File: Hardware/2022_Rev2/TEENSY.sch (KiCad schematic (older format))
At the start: 1 part

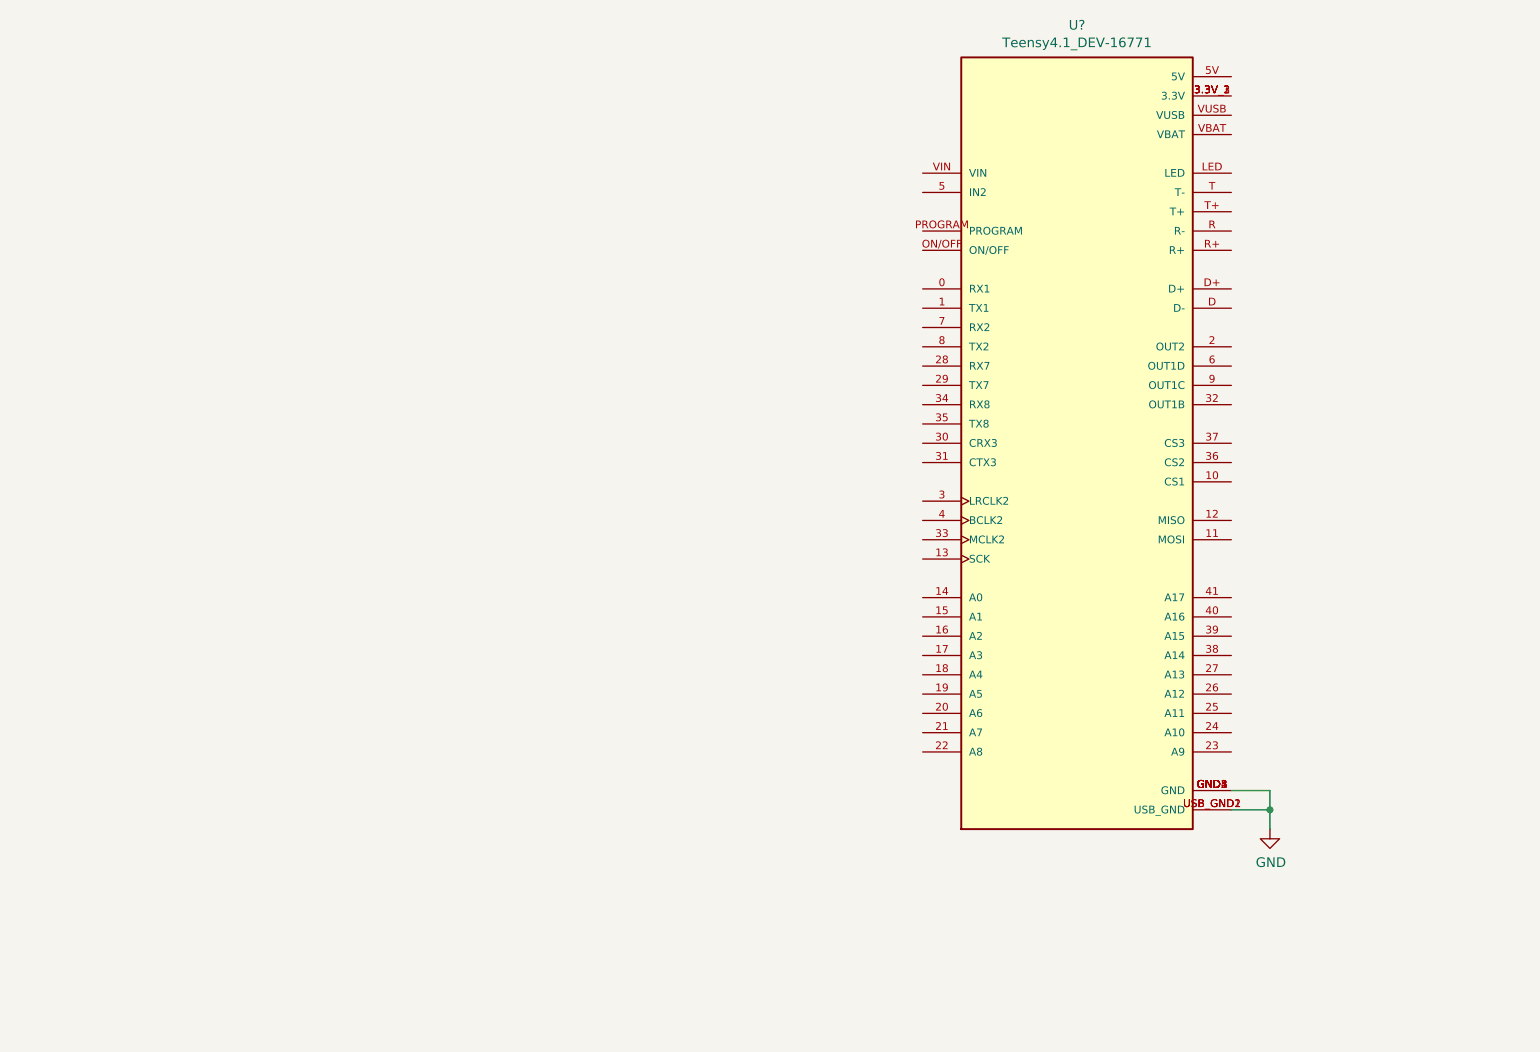
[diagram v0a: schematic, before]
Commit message: Organized some stuff and added Teensy connections
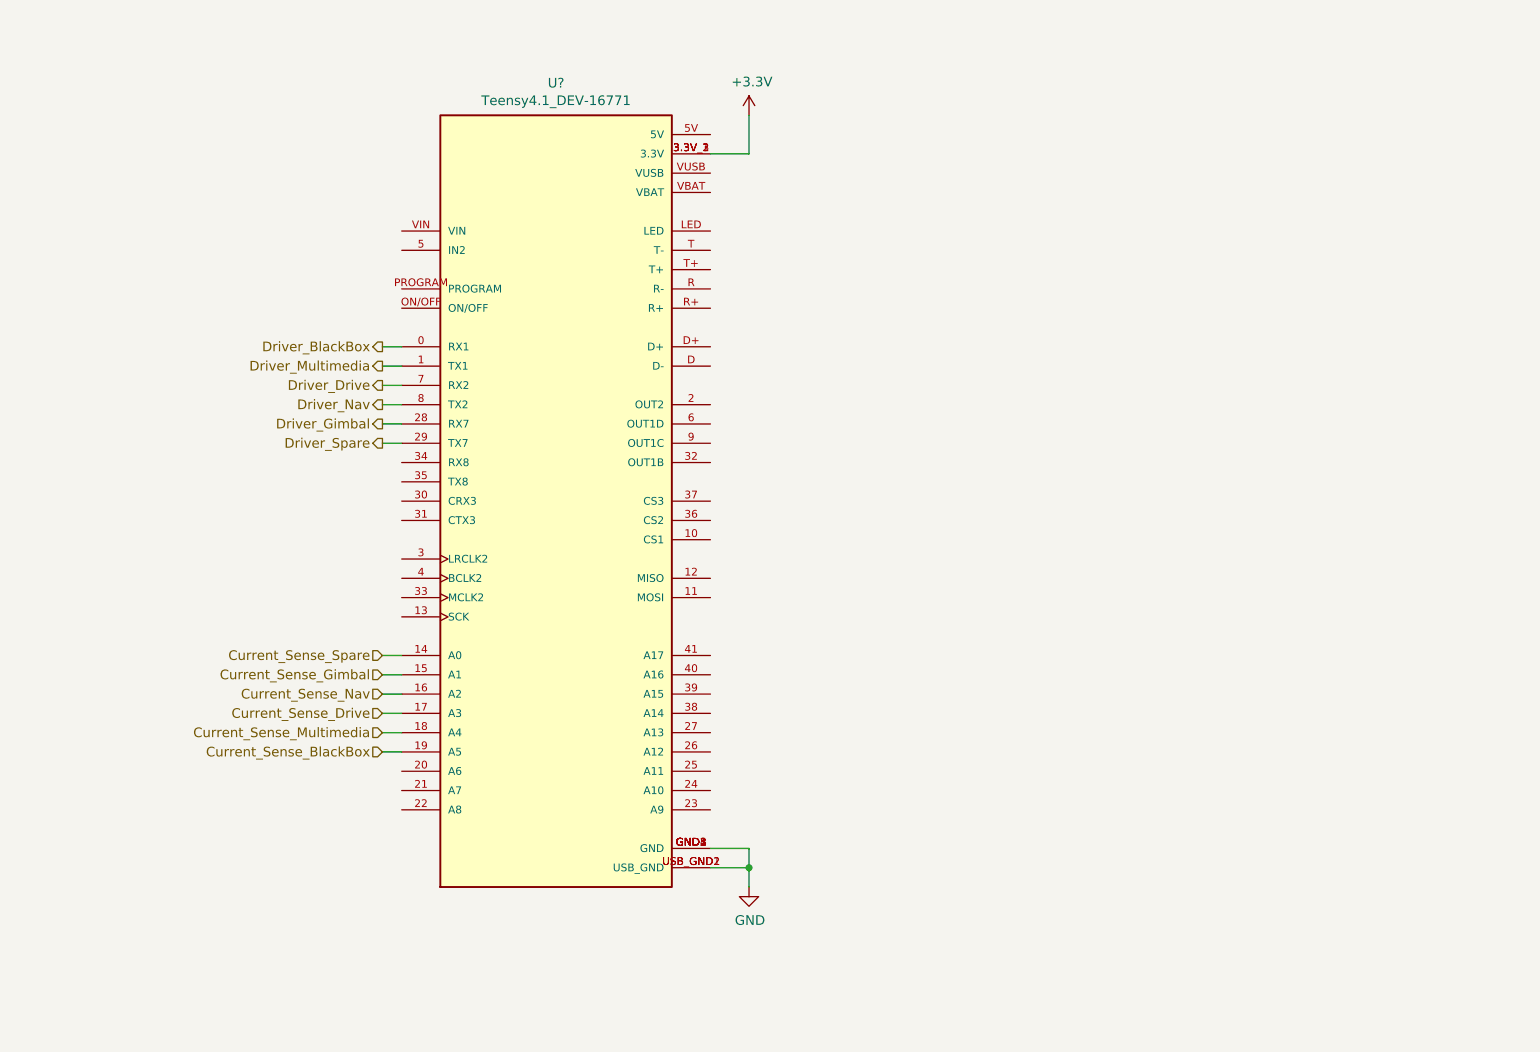
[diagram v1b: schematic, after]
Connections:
- net Driver_BlackBox: now reaches U?.0 (RX1)
- net Driver_Multimedia: now reaches U?.1 (TX1)
- net Current_Sense_Spare: now reaches U?.14 (A0)
- net Current_Sense_Gimbal: now reaches U?.15 (A1)
- net Current_Sense_Nav: now reaches U?.16 (A2)
- net Current_Sense_Drive: now reaches U?.17 (A3)
- net Current_Sense_Multimedia: now reaches U?.18 (A4)
- net Current_Sense_BlackBox: now reaches U?.19 (A5)
- net Driver_Gimbal: now reaches U?.28 (RX7)
- net Driver_Spare: now reaches U?.29 (TX7)
- net +3V3: now reaches U?.3.3V_1 (3.3V), U?.3.3V_2 (3.3V), U?.3.3V_3 (3.3V)
- net Driver_Drive: now reaches U?.7 (RX2)
- net Driver_Nav: now reaches U?.8 (TX2)
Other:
- moved on the sheet: U?
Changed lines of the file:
@@
 EESchema Schematic File Version 4
+LIBS:2022_Rev2-cache
 EELAYER 30 0
 EELAYER END
@@
 L 2022_Rev2-rescue:Teensy4.1_DEV-16771-MRDT_Shields U?
 U 1 1 6211982F
-P 8000 3250
-F 0 "U?" H 8000 5417 50  0000 C CNN
-F 1 "Teensy4.1_DEV-16771" H 8000 5326 50  0000 C CNN
-F 2 "MODULE_DEV-16771" H 10100 2950 50  0001 L BNN
-F 3 "" H 8000 3250 50  0001 L BNN
-F 4 "Manufacturer recommendations" H 10100 2700 50  0001 L BNN "STANDARD"
-F 5 "4.07mm" H 10350 2500 50  0001 L BNN "MAXIMUM_PACKAGE_HEIGHT"
-F 6 "SparkFun Electronics" H 10300 2350 50  0001 L BNN "MANUFACTURER"
-F 7 "4.1" H 7700 1050 50  0001 L BNN "PARTREV"
-	1    8000 3250
+P 5300 3550
+F 0 "U?" H 5300 5717 50  0000 C CNN
+F 1 "Teensy4.1_DEV-16771" H 5300 5626 50  0000 C CNN
+F 2 "MODULE_DEV-16771" H 7400 3250 50  0001 L BNN
+F 3 "" H 5300 3550 50  0001 L BNN
+F 4 "Manufacturer recommendations" H 7400 3000 50  0001 L BNN "STANDARD"
+F 5 "4.07mm" H 7650 2800 50  0001 L BNN "MAXIMUM_PACKAGE_HEIGHT"
+F 6 "SparkFun Electronics" H 7600 2650 50  0001 L BNN "MANUFACTURER"
+F 7 "4.1" H 5000 1350 50  0001 L BNN "PARTREV"
+	1    5300 3550
 	1    0    0    -1
 $EndComp
@@
 L power:GND #PWR?
 U 1 1 62120694
-P 9000 5250
-F 0 "#PWR?" H 9000 5000 50  0001 C CNN
-F 1 "GND" H 9005 5077 50  0000 C CNN
-F 2 "" H 9000 5250 50  0001 C CNN
-F 3 "" H 9000 5250 50  0001 C CNN
-	1    9000 5250
+P 6300 5550
+F 0 "#PWR?" H 6300 5300 50  0001 C CNN
+F 1 "GND" H 6305 5377 50  0000 C CNN
+F 2 "" H 6300 5550 50  0001 C CNN
+F 3 "" H 6300 5550 50  0001 C CNN
+	1    6300 5550
 	1    0    0    -1
 $EndComp
 Wire Wire Line
-	8800 5050 9000 5050
+	6100 5350 6300 5350
 Wire Wire Line
-	9000 5050 9000 5150
+	6300 5350 6300 5450
 Wire Wire Line
-	8800 5150 9000 5150
-Connection ~ 9000 5150
+	6100 5450 6300 5450
+Connection ~ 6300 5450
 Wire Wire Line
-	9000 5150 9000 5250
+	6300 5450 6300 5550
+$Comp
+L power:+3.3V #PWR?
+U 1 1 6220549B
+P 6300 1550
+F 0 "#PWR?" H 6300 1400 50  0001 C CNN
+F 1 "+3.3V" H 6315 1723 50  0000 C CNN
+F 2 "" H 6300 1550 50  0001 C CNN
+F 3 "" H 6300 1550 50  0001 C CNN
+	1    6300 1550
+	1    0    0    -1
+$EndComp
+Wire Wire Line
+	6100 1750 6300 1750
+Wire Wire Line
+	6300 1750 6300 1550
+Text HLabel 4400 4850 0    50   Input ~ 0
+Current_Sense_BlackBox
+Text HLabel 4400 4750 0    50   Input ~ 0
+Current_Sense_Multimedia
+Text HLabel 4400 4650 0    50   Input ~ 0
+Current_Sense_Drive
+Text HLabel 4400 4550 0    50   Input ~ 0
+Current_Sense_Nav
+Text HLabel 4400 4450 0    50   Input ~ 0
+Current_Sense_Gimbal
+Text HLabel 4400 4350 0    50   Input ~ 0
+Current_Sense_Spare
+Wire Wire Line
+	4400 4350 4500 4350
+Wire Wire Line
+	4500 4450 4400 4450
+Wire Wire Line
+	4400 4550 4500 4550
+Wire Wire Line
+	4500 4650 4400 4650
+Wire Wire Line
+	4400 4750 4500 4750
+Wire Wire Line
+	4500 4850 4400 4850
+Text HLabel 4400 2750 0    50   Output ~ 0
+Driver_BlackBox
+Text HLabel 4400 2850 0    50   Output ~ 0
+Driver_Multimedia
+Text HLabel 4400 2950 0    50   Output ~ 0
+Driver_Drive
+Text HLabel 4400 3050 0    50   Output ~ 0
+Driver_Nav
+Text HLabel 4400 3150 0    50   Output ~ 0
+Driver_Gimbal
+Text HLabel 4400 3250 0    50   Output ~ 0
+Driver_Spare
+Wire Wire Line
+	4400 2750 4500 2750
+Wire Wire Line
+	4500 2850 4400 2850
+Wire Wire Line
+	4400 2950 4500 2950
+Wire Wire Line
+	4500 3050 4400 3050
+Wire Wire Line
+	4400 3150 4500 3150
+Wire Wire Line
+	4500 3250 4400 3250
 $EndSCHEMATC

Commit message: Tiva implementation
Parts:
- removed U?: Teensy4.1_DEV-16771, MODULE_DEV-16771, symbol 2022_Rev2-rescue:Teensy4.1_DEV-16771-MRDT_Shields
- added U? (x8): TM4C129E_Launchpad, symbol MRDT_Shields:TM4C129E_Launchpad
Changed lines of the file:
@@
 EESchema Schematic File Version 4
-LIBS:2022_Rev2-cache
 EELAYER 30 0
 EELAYER END
@@
 $EndDescr
 $Comp
-L 2022_Rev2-rescue:Teensy4.1_DEV-16771-MRDT_Shields U?
-U 1 1 6211982F
-P 5300 3550
-F 0 "U?" H 5300 5717 50  0000 C CNN
-F 1 "Teensy4.1_DEV-16771" H 5300 5626 50  0000 C CNN
-F 2 "MODULE_DEV-16771" H 7400 3250 50  0001 L BNN
-F 3 "" H 5300 3550 50  0001 L BNN
-F 4 "Manufacturer recommendations" H 7400 3000 50  0001 L BNN "STANDARD"
-F 5 "4.07mm" H 7650 2800 50  0001 L BNN "MAXIMUM_PACKAGE_HEIGHT"
-F 6 "SparkFun Electronics" H 7600 2650 50  0001 L BNN "MANUFACTURER"
-F 7 "4.1" H 5000 1350 50  0001 L BNN "PARTREV"
-	1    5300 3550
+L power:GND #PWR?
+U 1 1 62120694
+P 6450 5600
+F 0 "#PWR?" H 6450 5350 50  0001 C CNN
+F 1 "GND" H 6455 5427 50  0000 C CNN
+F 2 "" H 6450 5600 50  0001 C CNN
+F 3 "" H 6450 5600 50  0001 C CNN
+	1    6450 5600
+	1    0    0    -1
+$EndComp
+Wire Wire Line
+	6250 5400 6450 5400
+Wire Wire Line
+	6450 5400 6450 5500
+Wire Wire Line
+	6250 5500 6450 5500
+Connection ~ 6450 5500
+Wire Wire Line
+	6450 5500 6450 5600
+$Comp
+L power:+3.3V #PWR?
+U 1 1 6220549B
+P 6550 1500
+F 0 "#PWR?" H 6550 1350 50  0001 C CNN
+F 1 "+3.3V" H 6565 1673 50  0000 C CNN
+F 2 "" H 6550 1500 50  0001 C CNN
+F 3 "" H 6550 1500 50  0001 C CNN
+	1    6550 1500
+	1    0    0    -1
+$EndComp
+Wire Wire Line
+	6350 1700 6550 1700
+Wire Wire Line
+	6550 1700 6550 1500
+Text HLabel 3750 5150 0    50   Input ~ 0
+Current_Sense_BlackBox
+Text HLabel 3750 5050 0    50   Input ~ 0
+Current_Sense_Multimedia
+Text HLabel 3750 4950 0    50   Input ~ 0
+Current_Sense_Drive
+Text HLabel 3750 4850 0    50   Input ~ 0
+Current_Sense_Nav
+Text HLabel 3750 4750 0    50   Input ~ 0
+Current_Sense_Gimbal
+Text HLabel 3750 4650 0    50   Input ~ 0
+Current_Sense_Spare
+Wire Wire Line
+	3750 4650 3850 4650
+Wire Wire Line
+	3850 4750 3750 4750
+Wire Wire Line
+	3750 4850 3850 4850
+Wire Wire Line
+	3850 4950 3750 4950
+Wire Wire Line
+	3750 5050 3850 5050
+Wire Wire Line
+	3850 5150 3750 5150
+Text HLabel 3750 3050 0    50   Output ~ 0
+Driver_BlackBox
+Text HLabel 3750 3150 0    50   Output ~ 0
+Driver_Multimedia
+Text HLabel 3750 3250 0    50   Output ~ 0
+Driver_Drive
+Text HLabel 3750 3350 0    50   Output ~ 0
+Driver_Nav
+Text HLabel 3750 3450 0    50   Output ~ 0
+Driver_Gimbal
+Text HLabel 3750 3550 0    50   Output ~ 0
+Driver_Spare
+Wire Wire Line
+	3750 3050 3850 3050
+Wire Wire Line
+	3850 3150 3750 3150
+Wire Wire Line
+	3750 3250 3850 3250
+Wire Wire Line
+	3850 3350 3750 3350
+Wire Wire Line
+	3750 3450 3850 3450
+Wire Wire Line
+	3850 3550 3750 3550
+$Comp
+L MRDT_Shields:TM4C129E_Launchpad U?
+U 1 1 622A6302
+P 5000 3300
+F 0 "U?" H 5301 3898 60  0000 L CNN
+F 1 "TM4C129E_Launchpad" H 5301 3792 60  0000 L CNN
+F 2 "" H 5000 3300 60  0001 C CNN
+F 3 "" H 5000 3300 60  0001 C CNN
+	1    5000 3300
 	1    0    0    -1
 $EndComp
 $Comp
-L power:GND #PWR?
-U 1 1 62120694
-P 6300 5550
-F 0 "#PWR?" H 6300 5300 50  0001 C CNN
-F 1 "GND" H 6305 5377 50  0000 C CNN
-F 2 "" H 6300 5550 50  0001 C CNN
-F 3 "" H 6300 5550 50  0001 C CNN
-	1    6300 5550
+L MRDT_Shields:TM4C129E_Launchpad U?
+U 2 1 622A854E
+P 6700 3250
+F 0 "U?" H 6731 4527 60  0000 C CNN
+F 1 "TM4C129E_Launchpad" H 6731 4421 60  0000 C CNN
+F 2 "" H 6700 3250 60  0001 C CNN
+F 3 "" H 6700 3250 60  0001 C CNN
+	2    6700 3250
+	-1   0    0    -1
+$EndComp
+$Comp
+L MRDT_Shields:TM4C129E_Launchpad U?
+U 3 1 622AA5F6
+P 7950 3250
+F 0 "U?" H 8255 3848 60  0000 L CNN
+F 1 "TM4C129E_Launchpad" H 8255 3742 60  0000 L CNN
+F 2 "" H 7950 3250 60  0001 C CNN
+F 3 "" H 7950 3250 60  0001 C CNN
+	3    7950 3250
 	1    0    0    -1
 $EndComp
-Wire Wire Line
-	6100 5350 6300 5350
-Wire Wire Line
-	6300 5350 6300 5450
-Wire Wire Line
-	6100 5450 6300 5450
-Connection ~ 6300 5450
-Wire Wire Line
-	6300 5450 6300 5550
 $Comp
-L power:+3.3V #PWR?
-U 1 1 6220549B
-P 6300 1550
-F 0 "#PWR?" H 6300 1400 50  0001 C CNN
-F 1 "+3.3V" H 6315 1723 50  0000 C CNN
-F 2 "" H 6300 1550 50  0001 C CNN
-F 3 "" H 6300 1550 50  0001 C CNN
-	1    6300 1550
+L MRDT_Shields:TM4C129E_Launchpad U?
+U 4 1 622AE2B5
+P 9800 3200
+F 0 "U?" H 9831 4477 60  0000 C CNN
+F 1 "TM4C129E_Launchpad" H 9831 4371 60  0000 C CNN
+F 2 "" H 9800 3200 60  0001 C CNN
+F 3 "" H 9800 3200 60  0001 C CNN
+	4    9800 3200
+	-1   0    0    -1
+$EndComp
+$Comp
+L MRDT_Shields:TM4C129E_Launchpad U?
+U 5 1 622B0F3D
+P 5000 4650
+F 0 "U?" H 5301 5248 60  0000 L CNN
+F 1 "TM4C129E_Launchpad" H 5301 5142 60  0000 L CNN
+F 2 "" H 5000 4650 60  0001 C CNN
+F 3 "" H 5000 4650 60  0001 C CNN
+	5    5000 4650
 	1    0    0    -1
 $EndComp
-Wire Wire Line
-	6100 1750 6300 1750
-Wire Wire Line
-	6300 1750 6300 1550
-Text HLabel 4400 4850 0    50   Input ~ 0
-Current_Sense_BlackBox
-Text HLabel 4400 4750 0    50   Input ~ 0
-Current_Sense_Multimedia
-Text HLabel 4400 4650 0    50   Input ~ 0
-Current_Sense_Drive
-Text HLabel 4400 4550 0    50   Input ~ 0
-Current_Sense_Nav
-Text HLabel 4400 4450 0    50   Input ~ 0
-Current_Sense_Gimbal
-Text HLabel 4400 4350 0    50   Input ~ 0
-Current_Sense_Spare
-Wire Wire Line
-	4400 4350 4500 4350
-Wire Wire Line
-	4500 4450 4400 4450
-Wire Wire Line
-	4400 4550 4500 4550
-Wire Wire Line
-	4500 4650 4400 4650
-Wire Wire Line
-	4400 4750 4500 4750
-Wire Wire Line
-	4500 4850 4400 4850
-Text HLabel 4400 2750 0    50   Output ~ 0
-Driver_BlackBox
-Text HLabel 4400 2850 0    50   Output ~ 0
-Driver_Multimedia
-Text HLabel 4400 2950 0    50   Output ~ 0
-Driver_Drive
-Text HLabel 4400 3050 0    50   Output ~ 0
-Driver_Nav
-Text HLabel 4400 3150 0    50   Output ~ 0
-Driver_Gimbal
-Text HLabel 4400 3250 0    50   Output ~ 0
-Driver_Spare
-Wire Wire Line
-	4400 2750 4500 2750
-Wire Wire Line
-	4500 2850 4400 2850
-Wire Wire Line
-	4400 2950 4500 2950
-Wire Wire Line
-	4500 3050 4400 3050
-Wire Wire Line
-	4400 3150 4500 3150
-Wire Wire Line
-	4500 3250 4400 3250
+$Comp
+L MRDT_Shields:TM4C129E_Launchpad U?
+U 6 1 622B4CAE
+P 6700 4700
+F 0 "U?" H 6731 5977 60  0000 C CNN
+F 1 "TM4C129E_Launchpad" H 6731 5871 60  0000 C CNN
+F 2 "" H 6700 4700 60  0001 C CNN
+F 3 "" H 6700 4700 60  0001 C CNN
+	6    6700 4700
+	-1   0    0    -1
+$EndComp
+$Comp
+L MRDT_Shields:TM4C129E_Launchpad U?
+U 7 1 622B6EBF
+P 7950 4750
+F 0 "U?" H 8255 5348 60  0000 L CNN
+F 1 "TM4C129E_Launchpad" H 8255 5242 60  0000 L CNN
+F 2 "" H 7950 4750 60  0001 C CNN
+F 3 "" H 7950 4750 60  0001 C CNN
+	7    7950 4750
+	1    0    0    -1
+$EndComp
+$Comp
+L MRDT_Shields:TM4C129E_Launchpad U?
+U 8 1 622B9460
+P 9750 4750
+F 0 "U?" H 9781 6027 60  0000 C CNN
+F 1 "TM4C129E_Launchpad" H 9781 5921 60  0000 C CNN
+F 2 "" H 9750 4750 60  0001 C CNN
+F 3 "" H 9750 4750 60  0001 C CNN
+	8    9750 4750
+	-1   0    0    -1
+$EndComp
 $EndSCHEMATC
